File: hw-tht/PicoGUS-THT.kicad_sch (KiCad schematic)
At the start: 38 parts, among them J1 IRQDMA_JP, J3 Bus_ISA_8bit, J5 SJ1-3535NG, J6 UART_TX, J7 USB power jumper, U1 Pico, U10 74AHCT126, U2 74AHC244, U3 SN74CB3T3257, U4 SN74CB3T3257, U5 74AHC14, U6 74AHC00, U7 74AHC00, U8 APS6404L-3SQR-SN

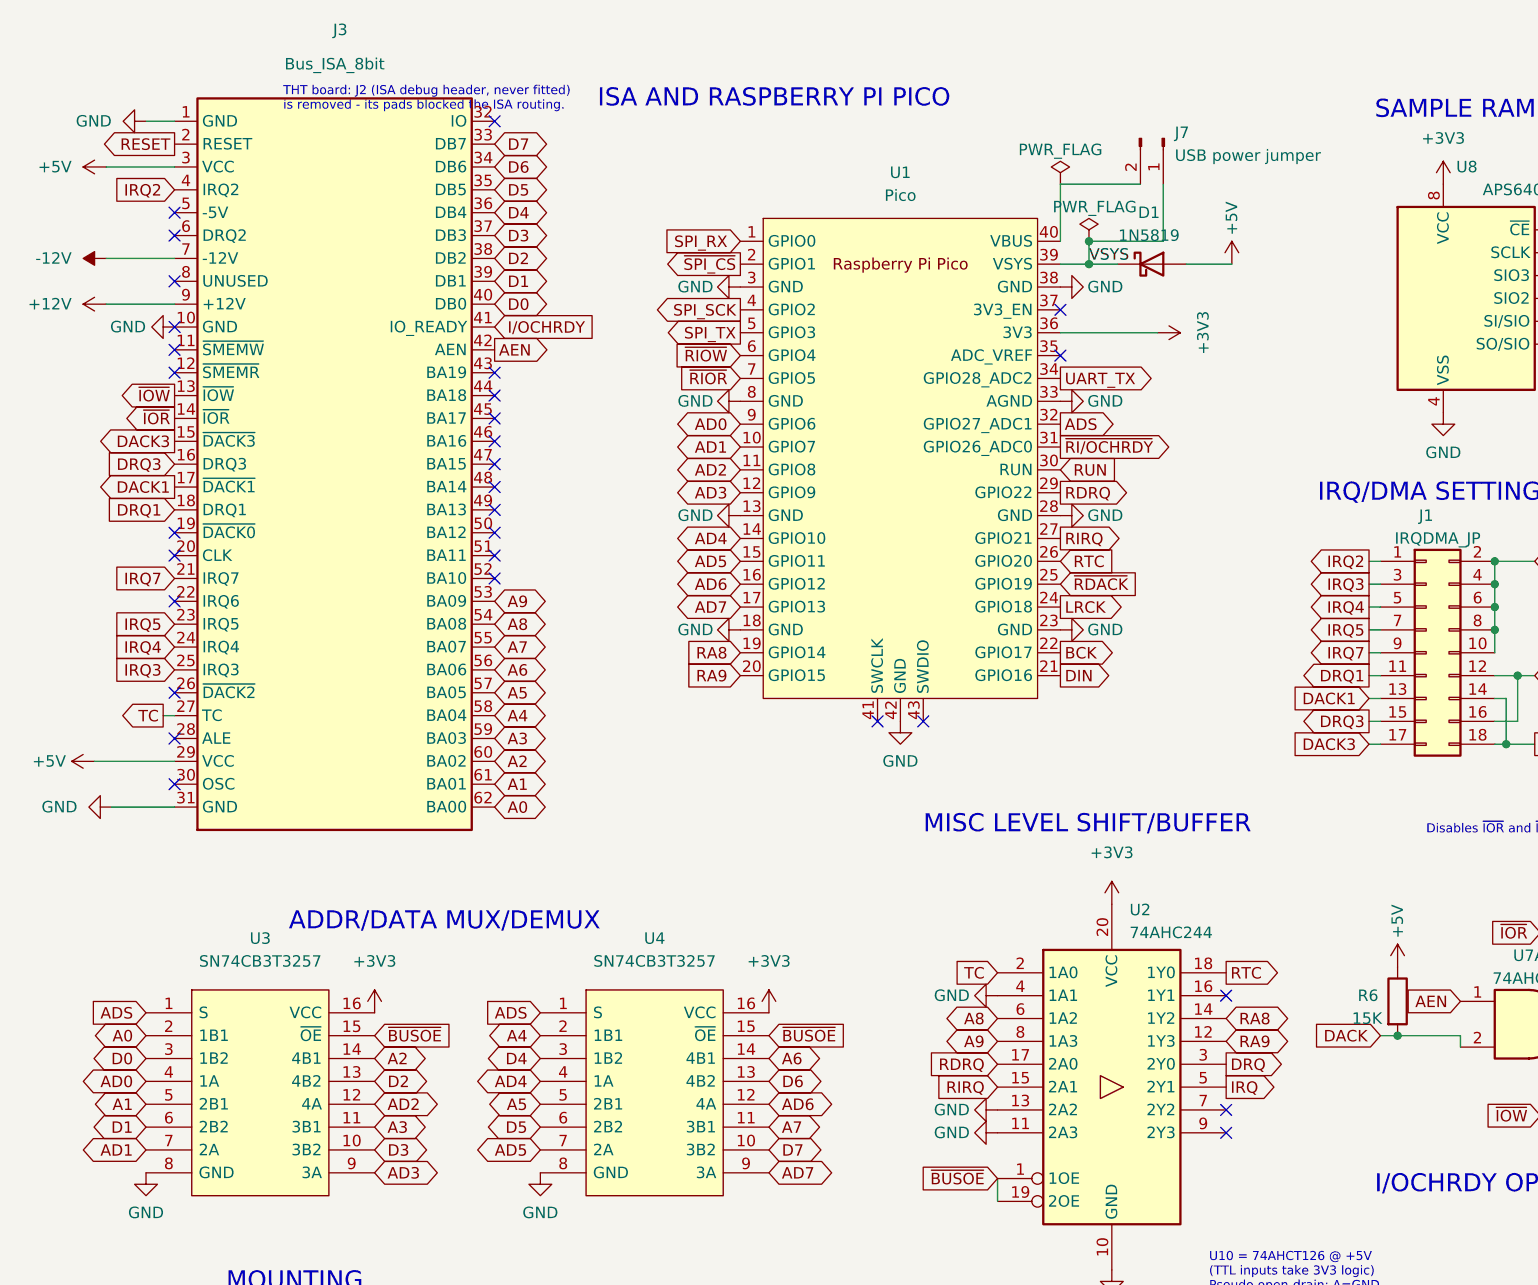
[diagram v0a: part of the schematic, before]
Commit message: Experimental 2nd IRQ (J10/J11), DMA label fix, labels grouped
- U2's spare channel (2A2 pin 13 -> 2Y2 pin 7, same drive and ~BUSOE as the
  IRQ output) now drives an optional second IRQ: J10 (next to the PSRAM,
  short stub on the fast SPI line) links GPIO3/SPI_TX to 2A2, R25 (10k)
  holds it low when open; J11 (next to J1) links 2Y2 to ISA IRQ3.
  GPIO3 is the PSRAM SPI_TX (all 26 Pico GPIOs are used), so this is for
  firmware that leaves the PSRAM idle. THT and SMD, ERC 0 errors.
- DMA heading moved back beside IRQ above J1.
- Silkscreen labels are members of their circuit-block KiCad groups
  (DAC, MIXER, AUDIO OUT, WT VOL, WAVEBLASTER, MIDI OUT, TX/USBPWR,
  IRQ/DMA + jumper numbers + divider, 2ND IRQ).
- Both boards re-routed: 0 DRC errors, 0 unconnected, schematic parity OK.
- BOMs: R25, J10/J11 (from the 1x40 strip), 6 jumper shunts.

Co-Authored-By: Claude Opus 5.5 <noreply@anthropic.com>
Claude-Session: https://claude.ai/code/session_011utN3x8yYUNDvkpGCEq5yD
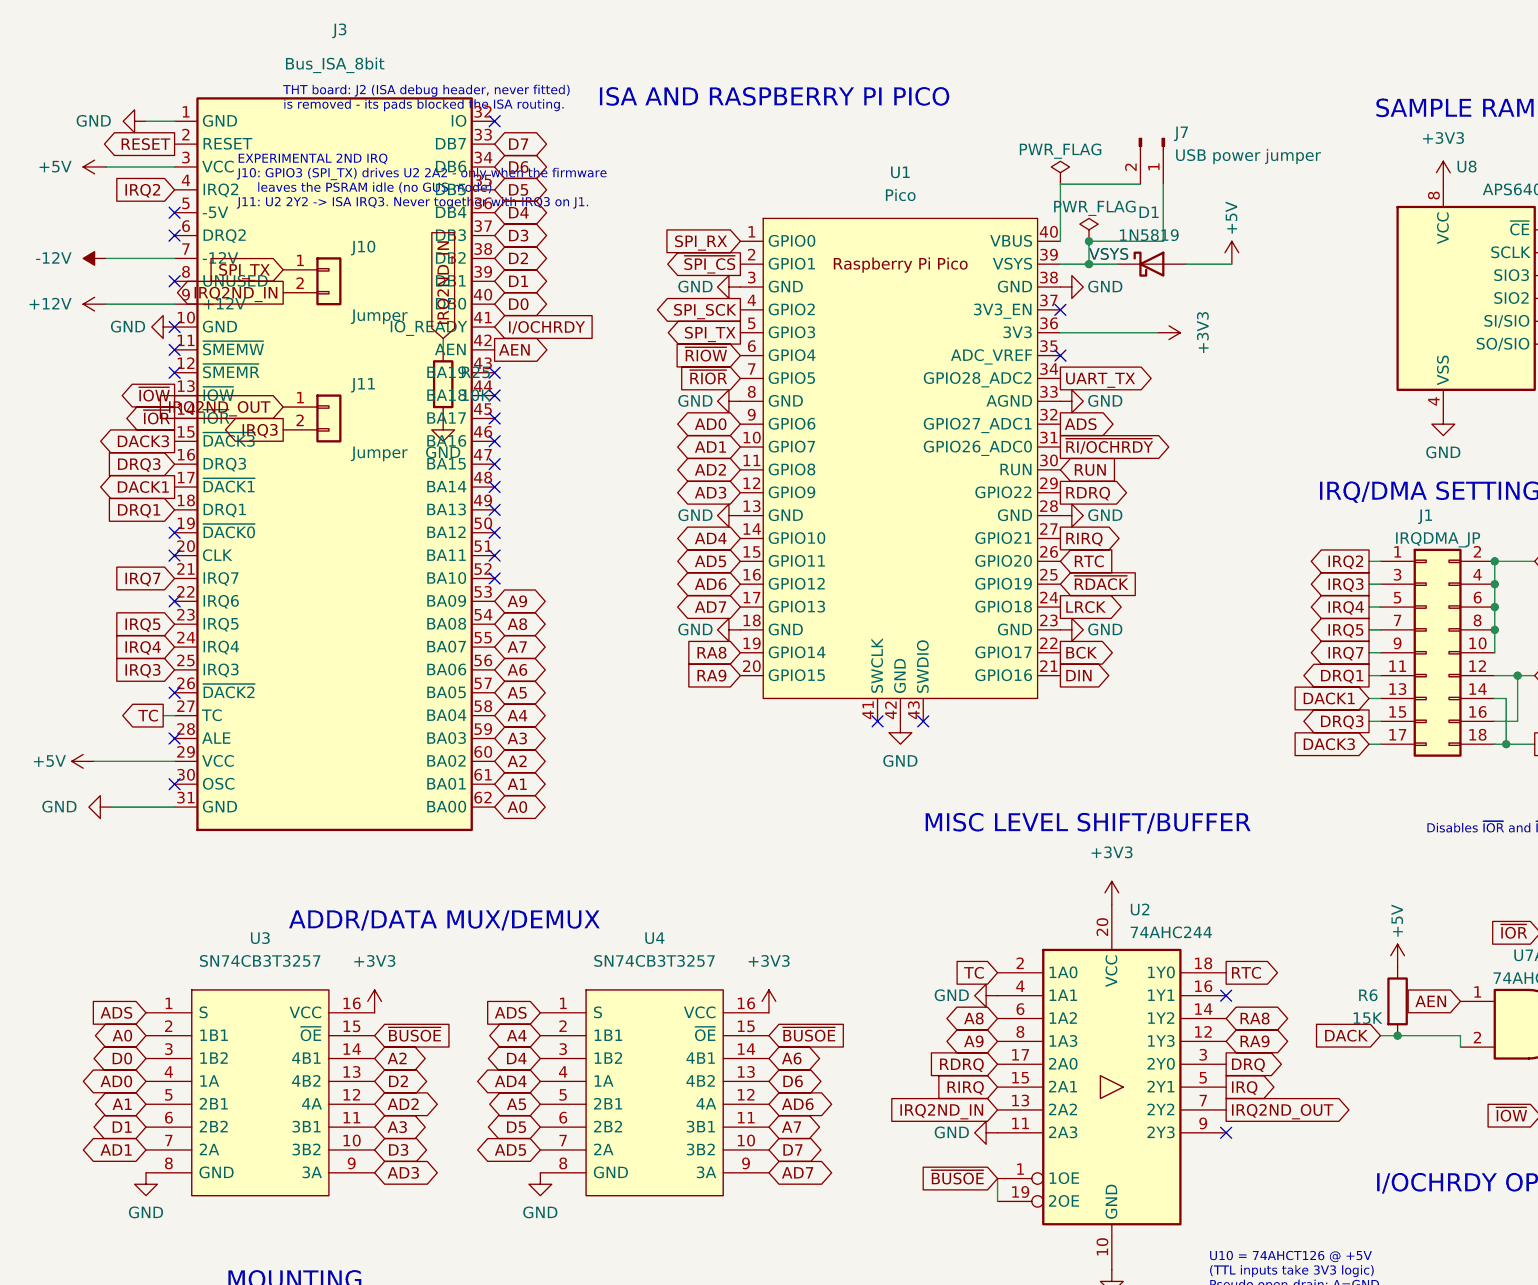
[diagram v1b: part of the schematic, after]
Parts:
- added J10, J11: Jumper, Connector_PinHeader_2.54mm:PinHeader_1x02_P2.54mm_Vertical, symbol Connector_Generic:Conn_01x02
- added R25: 10K, Resistor_THT:R_Axial_DIN0207_L6.3mm_D2.5mm_P10.16mm_Horizontal, symbol Device:R
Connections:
- net GND: now also R25.2; no longer U2.13 (2A2)
- net IRQ3: now also J11.2 (Pin_2)
- net SPI_TX: now also J10.1 (Pin_1)
- net IRQ2ND_OUT: now reaches U2.7 (2Y2)
- net IRQ2ND_OUT: now also J11.1 (Pin_1)
- new net IRQ2ND_IN: J10.2 (Pin_2), R25.1, U2.13 (2A2)
- no-connect marks 32 -> 31
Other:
- note added: "EXPERIMENTAL 2ND IRQ J10: GPIO3 (SPI_TX) drives U2 2A2 - only when the firmware leaves the PSRAM idle (no GUS mode) J11: U2 2Y2 -> ISA IRQ3. Never together with IRQ3 on J1."

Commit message: v1.3.0: drop the experimental 2nd IRQ; back-side artwork; label clean-up
- Experimental second IRQ removed from both boards: J10, J11 and R25 are gone,
  U2 pin 13 is tied to GND again and pin 7 is unconnected, as on v1.2.
  BOMs and DigiKey upload CSVs: one 10k less, 4 jumper shunts.
- Back silkscreen: the "Mila and Alisa" artwork (hw-common/art/mila-alisa.svg)
  with the dedication below it, mirrored so it reads from the back. On THT it
  is cut out 0.3 mm around every pad and hole, and the dedication sits in the
  one pad-free strip.
- Reference labels: U3/U4 horizontal under the chips; jumper labels J1/J6/J7
  upright; round capacitor labels (C1, C2, C22, C23, C32, C33) moved to free
  spots; the J3 (ISA fingers) label is hidden.
- Both boards: 0 DRC errors, 0 unconnected, schematic parity OK; ERC 0 errors.

Co-Authored-By: Claude Opus 5.5 <noreply@anthropic.com>
Claude-Session: https://claude.ai/code/session_011utN3x8yYUNDvkpGCEq5yD
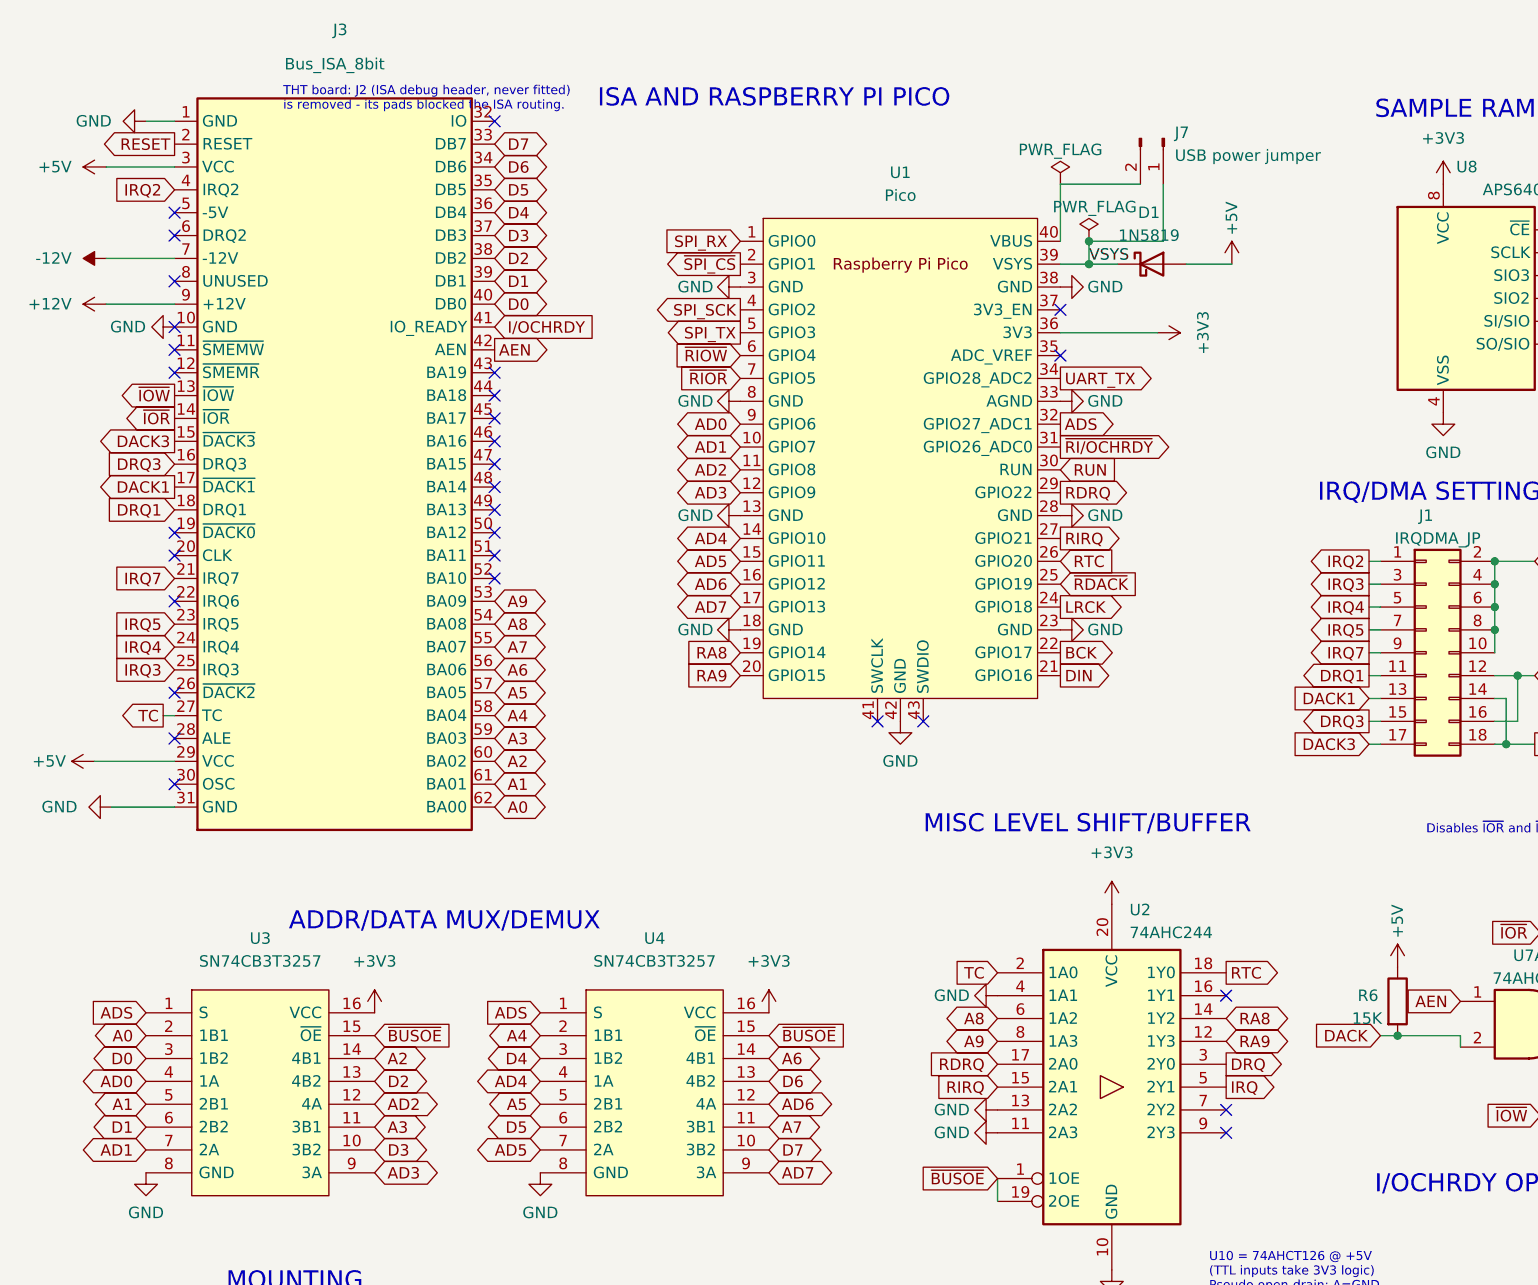
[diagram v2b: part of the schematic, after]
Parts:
- removed J10, J11: Jumper, Connector_PinHeader_2.54mm:PinHeader_1x02_P2.54mm_Vertical, symbol Connector_Generic:Conn_01x02
- removed R25: 10K, Resistor_THT:R_Axial_DIN0207_L6.3mm_D2.5mm_P10.16mm_Horizontal, symbol Device:R
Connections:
- net IRQ2ND_IN is gone; now on net GND: U2.13 (2A2)
- net IRQ2ND_OUT: no longer names the net of U2.7 (2Y2)
- no-connect marks 31 -> 32
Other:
- note removed: "EXPERIMENTAL 2ND IRQ J10: GPIO3 (SPI_TX) drives U2 2A2 - only when the firmware leaves the PSRAM idle (no GUS mode) J11: U2 2Y2 -> ISA IRQ3. Never together with IRQ3 on J1."
